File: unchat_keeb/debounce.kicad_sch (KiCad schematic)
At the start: 19 parts, among them U7 74HC14

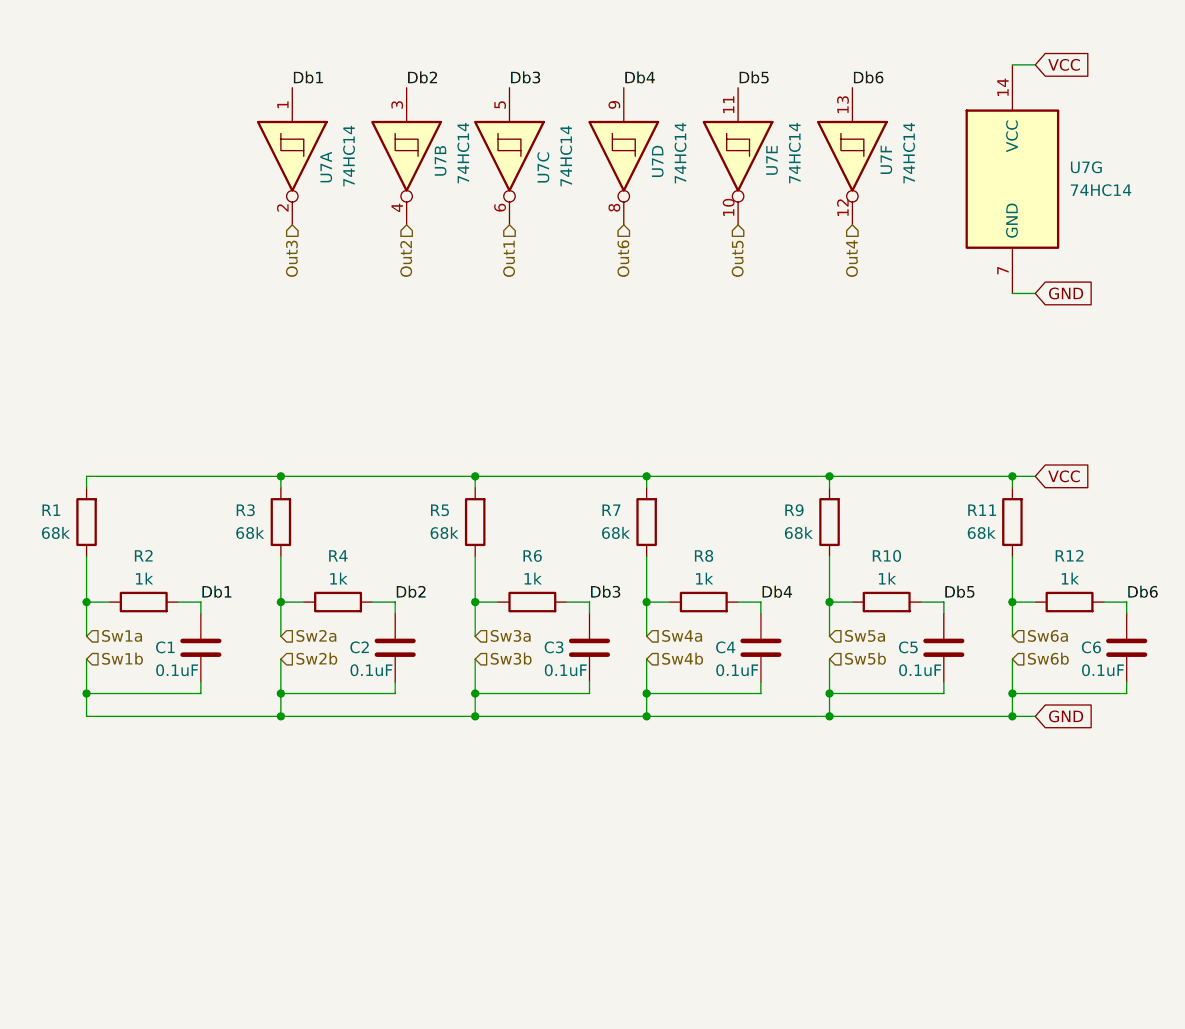
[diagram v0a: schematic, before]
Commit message: Add extra columns, updating to 42-key design
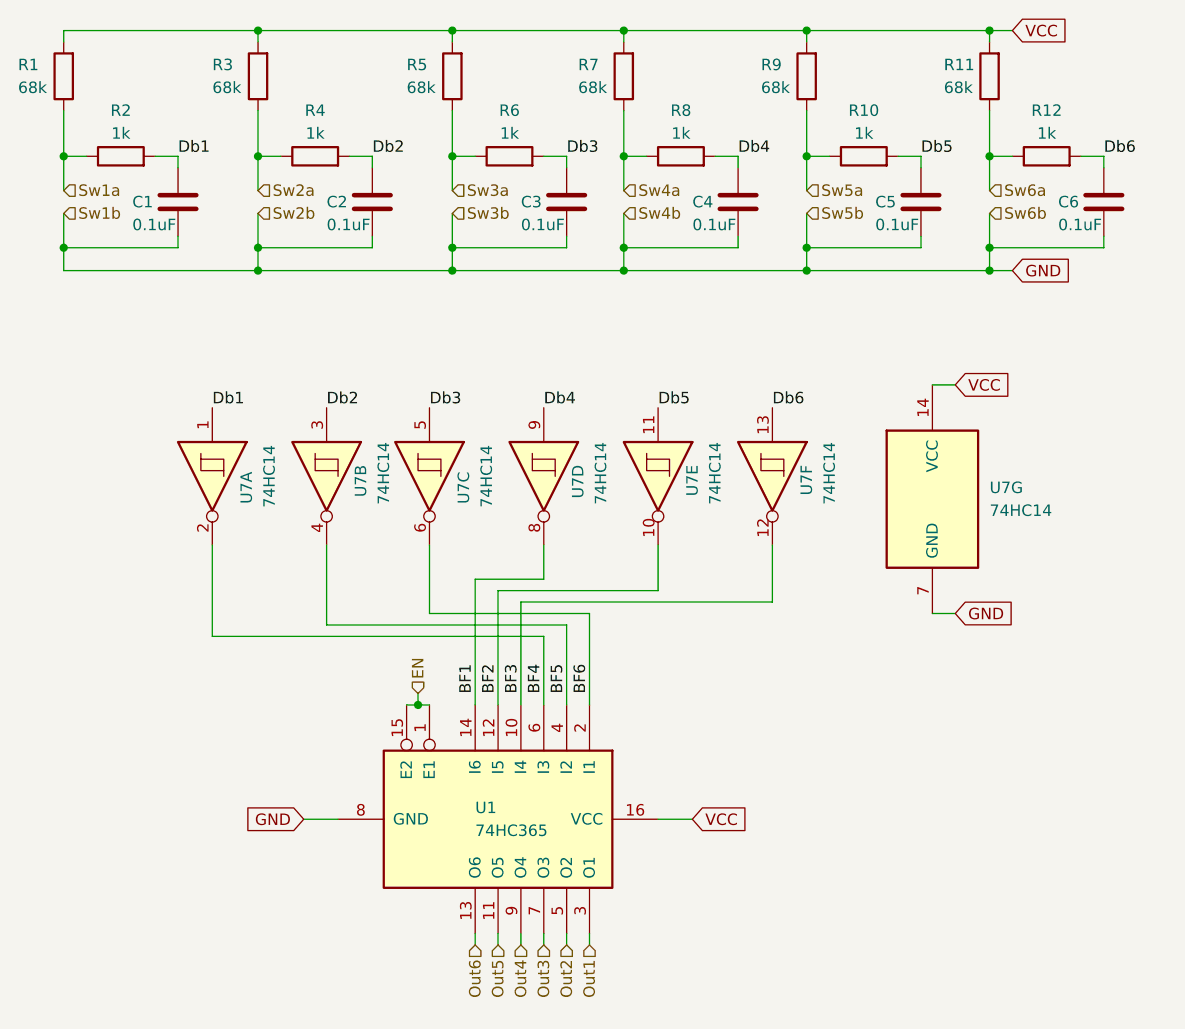
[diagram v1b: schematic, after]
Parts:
- added U1: 74HC365, Package_SO:TSSOP-16_4.4x5mm_P0.65mm, symbol 74xx:74LS365
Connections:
- net GND: now also U1.8 (GND)
- net Out1: now also U1.3 (O1); no longer U7.6
- net Out2: now also U1.5 (O2); no longer U7.4
- net Out3: now also U1.7 (O3); no longer U7.2
- net Out4: now also U1.9 (O4); no longer U7.12
- net Out5: now also U1.11 (O5); no longer U7.10
- net Out6: now also U1.13 (O6); no longer U7.8
- net VCC: now also U1.16 (VCC)
- new net BF1: U1.14 (I6), U7.8
- new net BF2: U1.12 (I5), U7.10
- new net BF3: U1.10 (I4), U7.12
- new net BF4: U1.6 (I3), U7.2
- new net BF5: U1.4 (I2), U7.4
- new net BF6: U1.2 (I1), U7.6
- new net EN: U1.1 (E1), U1.15 (E2)
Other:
- moved on the sheet: C1, C2, C3, C4, C5, C6, R1, R10, R11, R12, R2, R3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

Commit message: Add dxf layout and finish half keyboard pbc layout
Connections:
- net Db1: now also U7.9; no longer U7.1
- net Db2: now also U7.11; no longer U7.3
- net Db3: now also U7.13; no longer U7.5
- net Db4: now also U7.1; no longer U7.9
- net Db5: now also U7.3; no longer U7.11
- net Db6: now also U7.5; no longer U7.13
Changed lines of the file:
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@@
     (stroke (width 0) (type default))
+  )
+  (label "Db3" (at 118.11 73.66 0) (fields_autoplaced)
+    (effects (font (size 1.27 1.27)) (justify left bottom))
+  )
+  (label "Db4" (at 55.88 73.66 0) (fields_autoplaced)
+    (effects (font (size 1.27 1.27)) (justify left bottom))
+  )
+  (label "Db1" (at 92.71 73.66 0) (fields_autoplaced)
+    (effects (font (size 1.27 1.27)) (justify left bottom))
   )
   (label "BF3" (at 90.17 105.41 90) (fields_autoplaced)
@@
     (effects (font (size 1.27 1.27)) (justify left bottom))
   )
-  (label "Db2" (at 68.58 73.66 0) (fields_autoplaced)
-    (effects (font (size 1.27 1.27)) (justify left bottom))
-  )
-  (label "Db6" (at 118.11 73.66 0) (fields_autoplaced)
+  (label "Db5" (at 68.58 73.66 0) (fields_autoplaced)
     (effects (font (size 1.27 1.27)) (justify left bottom))
   )
@@
     (effects (font (size 1.27 1.27)) (justify left bottom))
   )
-  (label "Db5" (at 105.41 73.66 0) (fields_autoplaced)
+  (label "Db5" (at 134.62 45.72 0) (fields_autoplaced)
     (effects (font (size 1.27 1.27)) (justify left bottom))
   )
-  (label "Db5" (at 134.62 45.72 0) (fields_autoplaced)
+  (label "Db2" (at 105.41 73.66 0) (fields_autoplaced)
     (effects (font (size 1.27 1.27)) (justify left bottom))
   )
@@
     (effects (font (size 1.27 1.27)) (justify left bottom))
   )
-  (label "Db3" (at 80.01 73.66 0) (fields_autoplaced)
-    (effects (font (size 1.27 1.27)) (justify left bottom))
-  )
-  (label "Db1" (at 55.88 73.66 0) (fields_autoplaced)
+  (label "Db6" (at 80.01 73.66 0) (fields_autoplaced)
     (effects (font (size 1.27 1.27)) (justify left bottom))
   )
@@
     (effects (font (size 1.27 1.27)) (justify left bottom))
   )
-  (label "Db4" (at 92.71 73.66 0) (fields_autoplaced)
-    (effects (font (size 1.27 1.27)) (justify left bottom))
-  )

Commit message: Finalize the board
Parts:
- U1: footprint Package_SO:TSSOP-16_4.4x5mm_P0.65mm -> GKanwarLibrary:TSSOP-16_4.4x5mm_P0.65mm
- U7: footprint Package_SO:TSSOP-14_4.4x5mm_P0.65mm -> GKanwarLibrary:TSSOP-14_4.4x5mm_P0.65mm
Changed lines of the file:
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@@
       (effects (font (size 1.27 1.27)) (justify left))
     )
-    (property "Footprint" "Package_SO:TSSOP-14_4.4x5mm_P0.65mm" (at 105.41 81.28 0)
+    (property "Footprint" "GKanwarLibrary:TSSOP-14_4.4x5mm_P0.65mm" (at 105.41 81.28 0)
       (effects (font (size 1.27 1.27)) hide)
     )
@@
       (effects (font (size 1.27 1.27)) (justify left))
     )
-    (property "Footprint" "Package_SO:TSSOP-14_4.4x5mm_P0.65mm" (at 68.58 81.28 0)
+    (property "Footprint" "GKanwarLibrary:TSSOP-14_4.4x5mm_P0.65mm" (at 68.58 81.28 0)
       (effects (font (size 1.27 1.27)) hide)
     )
@@
       (effects (font (size 1.27 1.27)))
     )
-    (property "Footprint" "Package_SO:TSSOP-14_4.4x5mm_P0.65mm" (at 55.88 81.28 0)
+    (property "Footprint" "GKanwarLibrary:TSSOP-14_4.4x5mm_P0.65mm" (at 55.88 81.28 0)
       (effects (font (size 1.27 1.27)) hide)
     )
@@
       (effects (font (size 1.27 1.27)) (justify left))
     )
-    (property "Footprint" "Package_SO:TSSOP-16_4.4x5mm_P0.65mm" (at 87.63 119.38 0)
+    (property "Footprint" "GKanwarLibrary:TSSOP-16_4.4x5mm_P0.65mm" (at 87.63 119.38 0)
       (effects (font (size 1.27 1.27)) hide)
     )
@@
       (effects (font (size 1.27 1.27)) (justify left))
     )
-    (property "Footprint" "Package_SO:TSSOP-14_4.4x5mm_P0.65mm" (at 92.71 81.28 0)
+    (property "Footprint" "GKanwarLibrary:TSSOP-14_4.4x5mm_P0.65mm" (at 92.71 81.28 0)
       (effects (font (size 1.27 1.27)) hide)
     )
@@
       (effects (font (size 1.27 1.27)))
     )
-    (property "Footprint" "Package_SO:TSSOP-14_4.4x5mm_P0.65mm" (at 80.01 81.28 0)
+    (property "Footprint" "GKanwarLibrary:TSSOP-14_4.4x5mm_P0.65mm" (at 80.01 81.28 0)
       (effects (font (size 1.27 1.27)) hide)
     )
@@
       (effects (font (size 1.27 1.27)) (justify left))
     )
-    (property "Footprint" "Package_SO:TSSOP-14_4.4x5mm_P0.65mm" (at 118.11 81.28 0)
+    (property "Footprint" "GKanwarLibrary:TSSOP-14_4.4x5mm_P0.65mm" (at 118.11 81.28 0)
       (effects (font (size 1.27 1.27)) hide)
     )
@@
       (effects (font (size 1.27 1.27)) (justify left))
     )
-    (property "Footprint" "Package_SO:TSSOP-14_4.4x5mm_P0.65mm" (at 135.89 83.82 0)
-      (effects (font (size 1.27 1.27)) hide)
-    )
+    (property "Footprint" "GKanwarLibrary:TSSOP-14_4.4x5mm_P0.65mm" (at 135.89 83.82 0)
+      (effects (font (size 1.27 1.27)) hide)
+    )
